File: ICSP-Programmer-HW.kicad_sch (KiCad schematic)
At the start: 0 parts

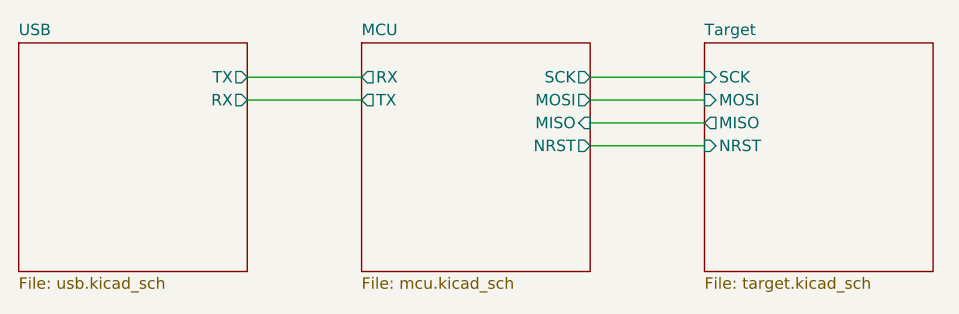
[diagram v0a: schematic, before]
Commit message: Fix direction issue on MISO/MOSI
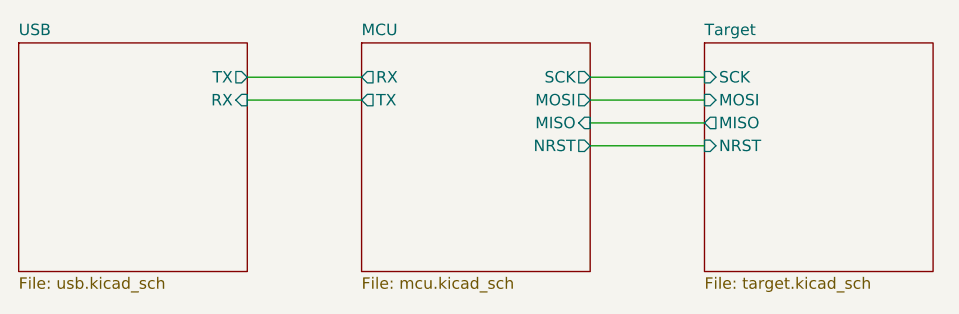
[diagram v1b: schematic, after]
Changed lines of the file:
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@@
       (effects (font (size 1.27 1.27)) (justify left top))
     )
-    (pin "RX" output (at 76.2 44.45 0)
+    (pin "RX" input (at 76.2 44.45 0)
       (effects (font (size 1.27 1.27)) (justify right))
     )
